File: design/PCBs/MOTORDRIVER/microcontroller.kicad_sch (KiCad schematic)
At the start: 0 parts

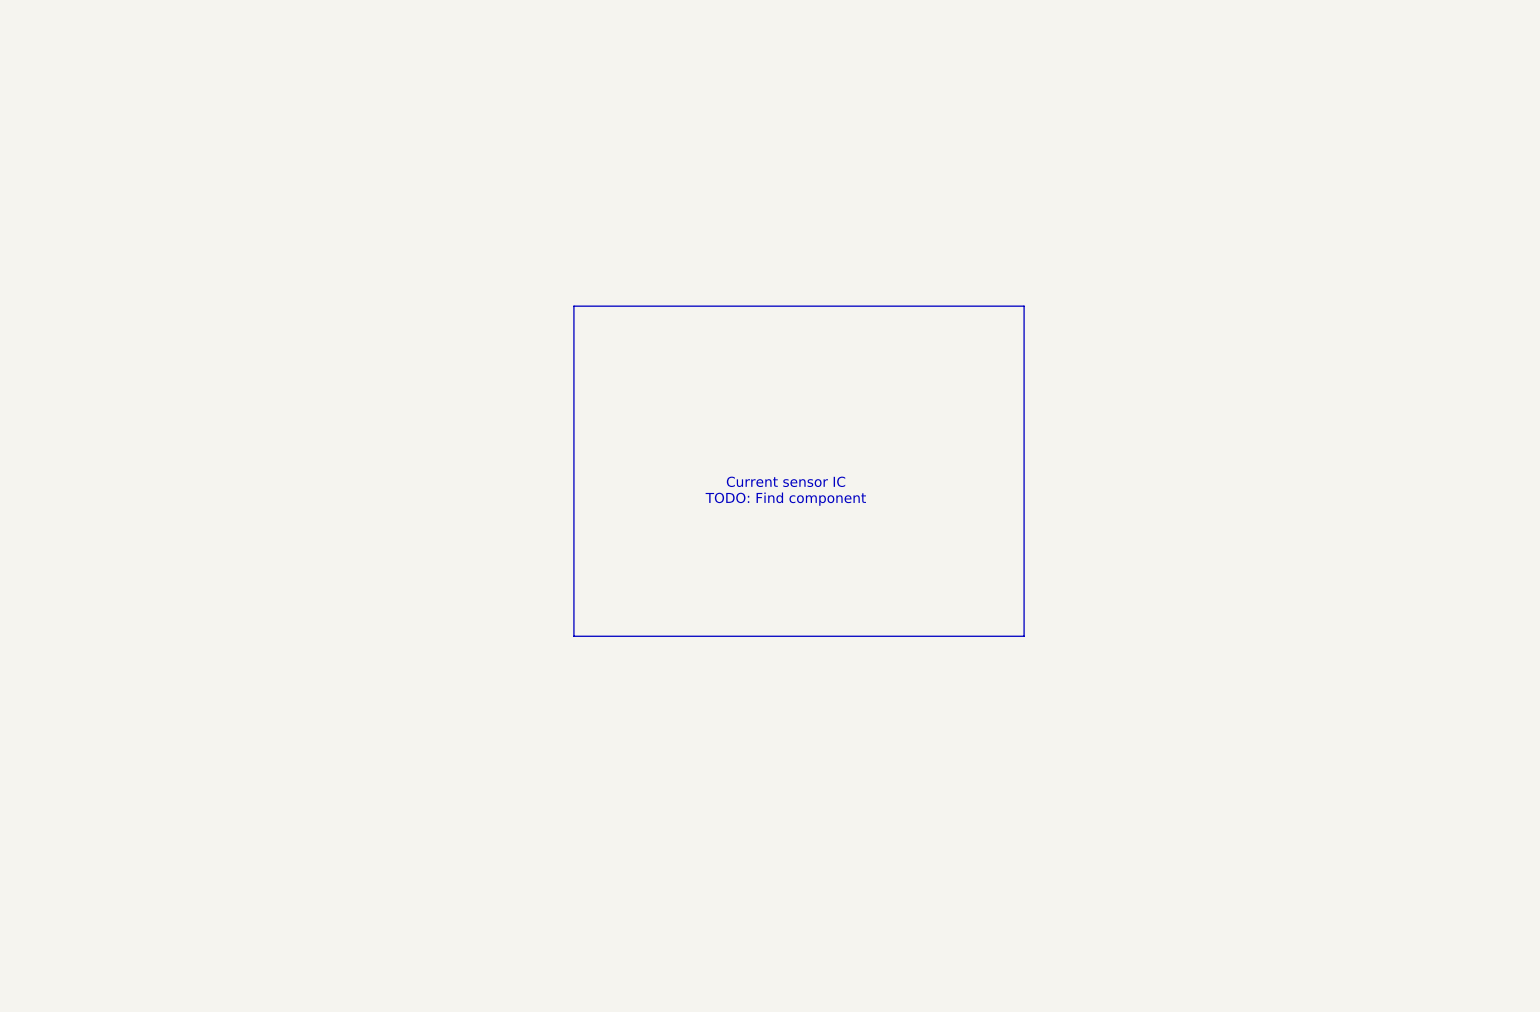
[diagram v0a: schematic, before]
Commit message: moved controller pcb to a single unified pcb, added more work on motordriver
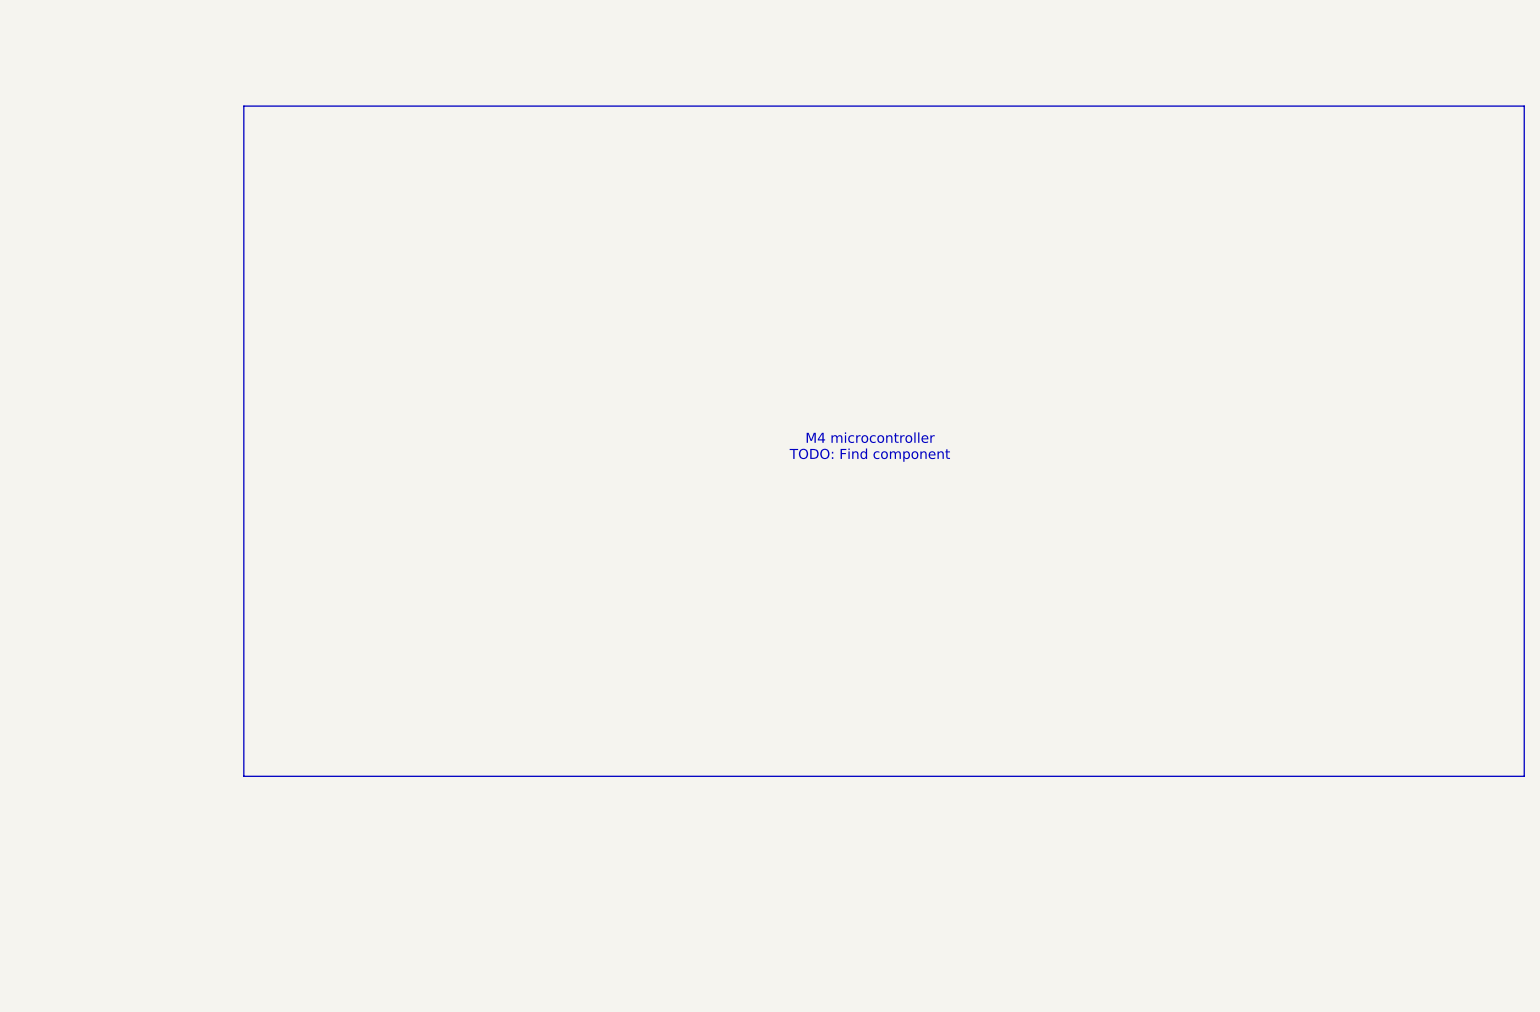
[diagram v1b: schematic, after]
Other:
- note added: "M4 microcontroller TODO: Find component"
- note removed: "Current sensor IC TODO: Find component"
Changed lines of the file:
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@@
 	(paper "A4")
 	(rectangle
-		(start 105.41 74.93)
-		(end 162.56 116.84)
+		(start 63.5 49.53)
+		(end 226.06 134.62)
 		(stroke
 			(width 0)
@@
 		)
 	)
-	(text "Current sensor IC\nTODO: Find component"
+	(text "M4 microcontroller\nTODO: Find component"
 		(exclude_from_sim no)
-		(at 132.334 98.552 0)
+		(at 143.002 92.964 0)
 		(effects
 			(font

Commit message: MCU added, x-ed some motordriver pins
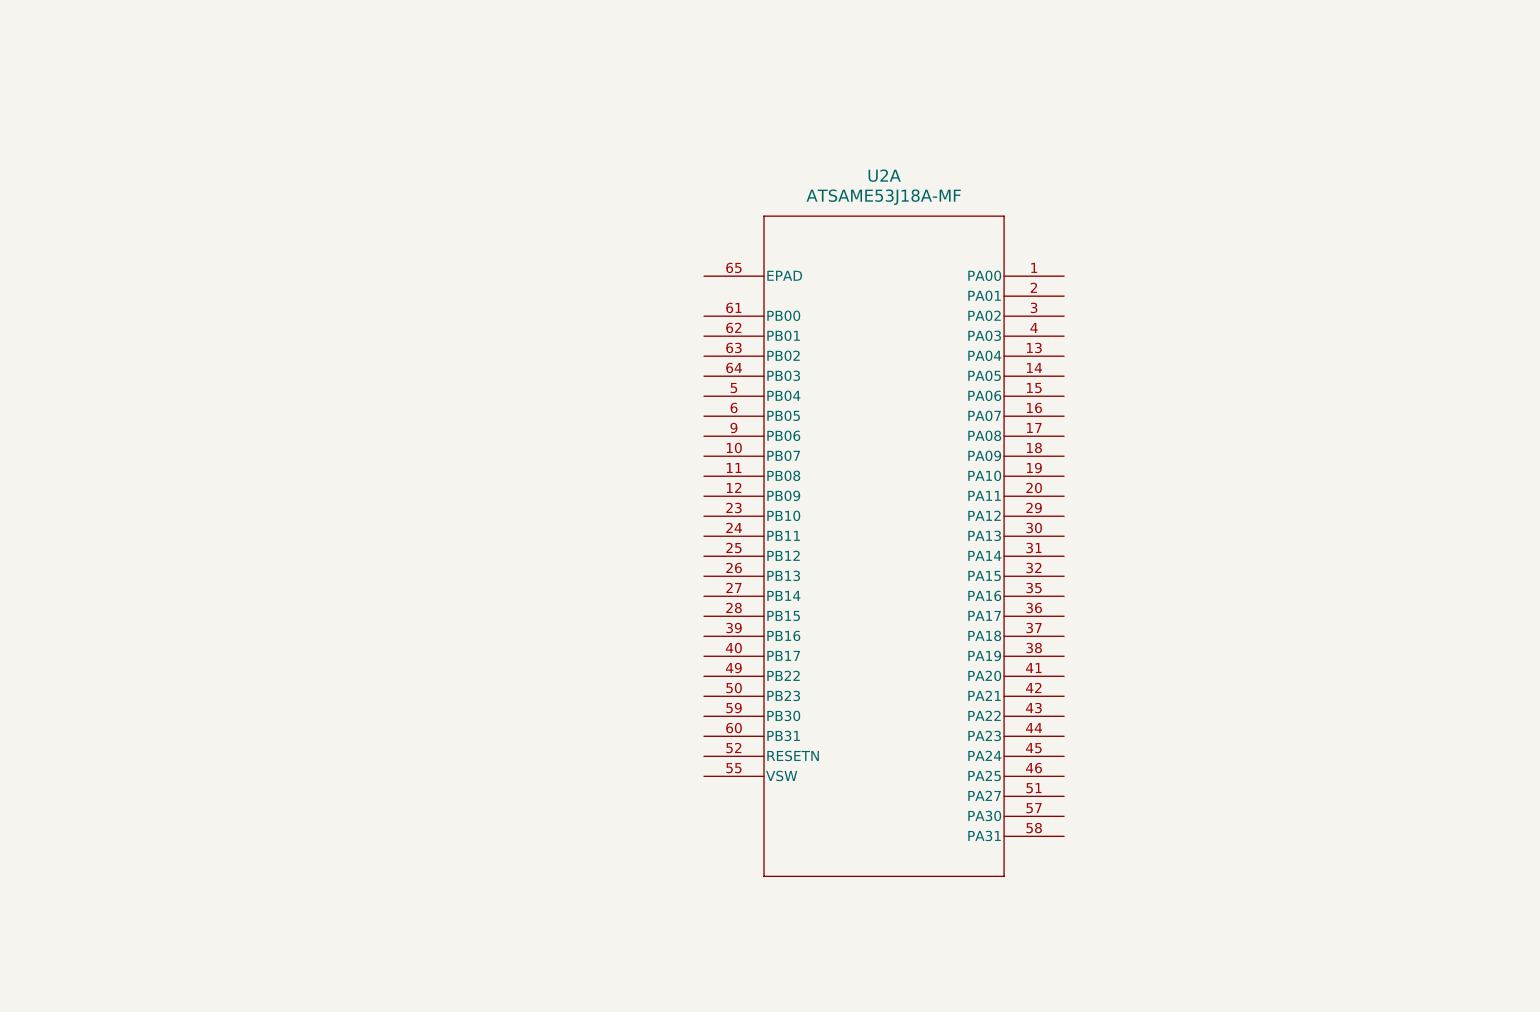
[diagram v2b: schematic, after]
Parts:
- added U2: ATSAME53J18A-MF, QFN64_9x9MC_MCH, symbol cortex-arm-m4:ATSAME53J18A-MF
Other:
- note removed: "M4 microcontroller TODO: Find component"
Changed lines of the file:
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@@
 	(generator_version "8.0")
 	(paper "A4")
-	(rectangle
-		(start 63.5 49.53)
-		(end 226.06 134.62)
-		(stroke
-			(width 0)
-			(type default)
-		)
-		(fill
-			(type none)
-		)
-	)
-	(text "M4 microcontroller\nTODO: Find component"
+	(symbol
+		(lib_id "cortex-arm-m4:ATSAME53J18A-MF")
+		(at 121.92 71.12 0)
+		(unit 1)
 		(exclude_from_sim no)
-		(at 143.002 92.964 0)
-		(effects
-			(font
-				(size 1.27 1.27)
+		(in_bom yes)
+		(on_board yes)
+		(dnp no)
+		(fields_autoplaced yes)
+		(property "Reference" "U2"
+			(at 144.78 58.42 0)
+			(effects
+				(font
+					(size 1.524 1.524)
+				)
 			)
 		)
+		(property "Value" "ATSAME53J18A-MF"
+			(at 144.78 60.96 0)
+			(effects
+				(font
+					(size 1.524 1.524)
+				)
+			)
+		)
+		(property "Footprint" "QFN64_9x9MC_MCH"
+			(at 121.92 71.12 0)
+			(effects
+				(font
+					(size 1.27 1.27)
+					(italic yes)
+				)
+				(hide yes)
+			)
+		)
+		(property "Datasheet" "ATSAME53J18A-MF"
+			(at 121.92 71.12 0)
+			(effects
+				(font
+					(size 1.27 1.27)
+					(italic yes)
+				)
+				(hide yes)
+			)
+		)
+		(property "Description" ""
+			(at 121.92 71.12 0)
+			(effects
+				(font
+					(size 1.27 1.27)
+				)
+				(hide yes)
+			)
+		)
+		(pin "60"
+		)
+		(pin "42"
+		)
+		(pin "59"
+		)
+		(pin "63"
+		)
+		(pin "50"
+		)
+		(pin "64"
+		)
+		(pin "62"
+		)
+		(pin "21"
+		)
+		(pin "61"
+		)
+		(pin "55"
+		)
+		(pin "65"
+		)
+		(pin "19"
+		)
+		(pin "22"
+		)
+		(pin "38"
+		)
+		(pin "52"
+		)
+		(pin "6"
+		)
+		(pin "18"
+		)
+		(pin "58"
+		)
+		(pin "1"
+		)
+		(pin "12"
+		)
+		(pin "11"
+		)
+		(pin "10"
+		)
+		(pin "2"
+		)
+		(pin "20"
+		)
+		(pin "57"
+		)
+		(pin "23"
+		)
+		(pin "44"
+		)
+		(pin "30"
+		)
+		(pin "13"
+		)
+		(pin "56"
+		)
+		(pin "43"
+		)
+		(pin "4"
+		)
+		(pin "32"
+		)
+		(pin "54"
+		)
+		(pin "15"
+		)
+		(pin "40"
+		)
+		(pin "8"
+		)
+		(pin "7"
+		)
+		(pin "45"
+		)
+		(pin "51"
+		)
+		(pin "3"
+		)
+		(pin "25"
+		)
+		(pin "27"
+		)
+		(pin "29"
+		)
+		(pin "33"
+		)
+		(pin "48"
+		)
+		(pin "14"
+		)
+		(pin "28"
+		)
+		(pin "53"
+		)
+		(pin "47"
+		)
+		(pin "34"
+		)
+		(pin "36"
+		)
+		(pin "49"
+		)
+		(pin "5"
+		)
+		(pin "46"
+		)
+		(pin "9"
+		)
+		(pin "26"
+		)
+		(pin "31"
+		)
+		(pin "35"
+		)
+		(pin "17"
+		)
+		(pin "37"
+		)
+		(pin "16"
+		)
+		(pin "24"
+		)
+		(pin "41"
+		)
+		(pin "39"
+		)
+		(instances
+			(project ""
+				(path "/c7634e88-16d1-45ec-9aac-9c841e03cf6d/9ebbb593-eaf1-4a56-ba2a-164e20b1d55e"
+					(reference "U2")
+					(unit 1)
+				)
+			)
+		)

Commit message: cortex added, fixed some symbols in motordriver file
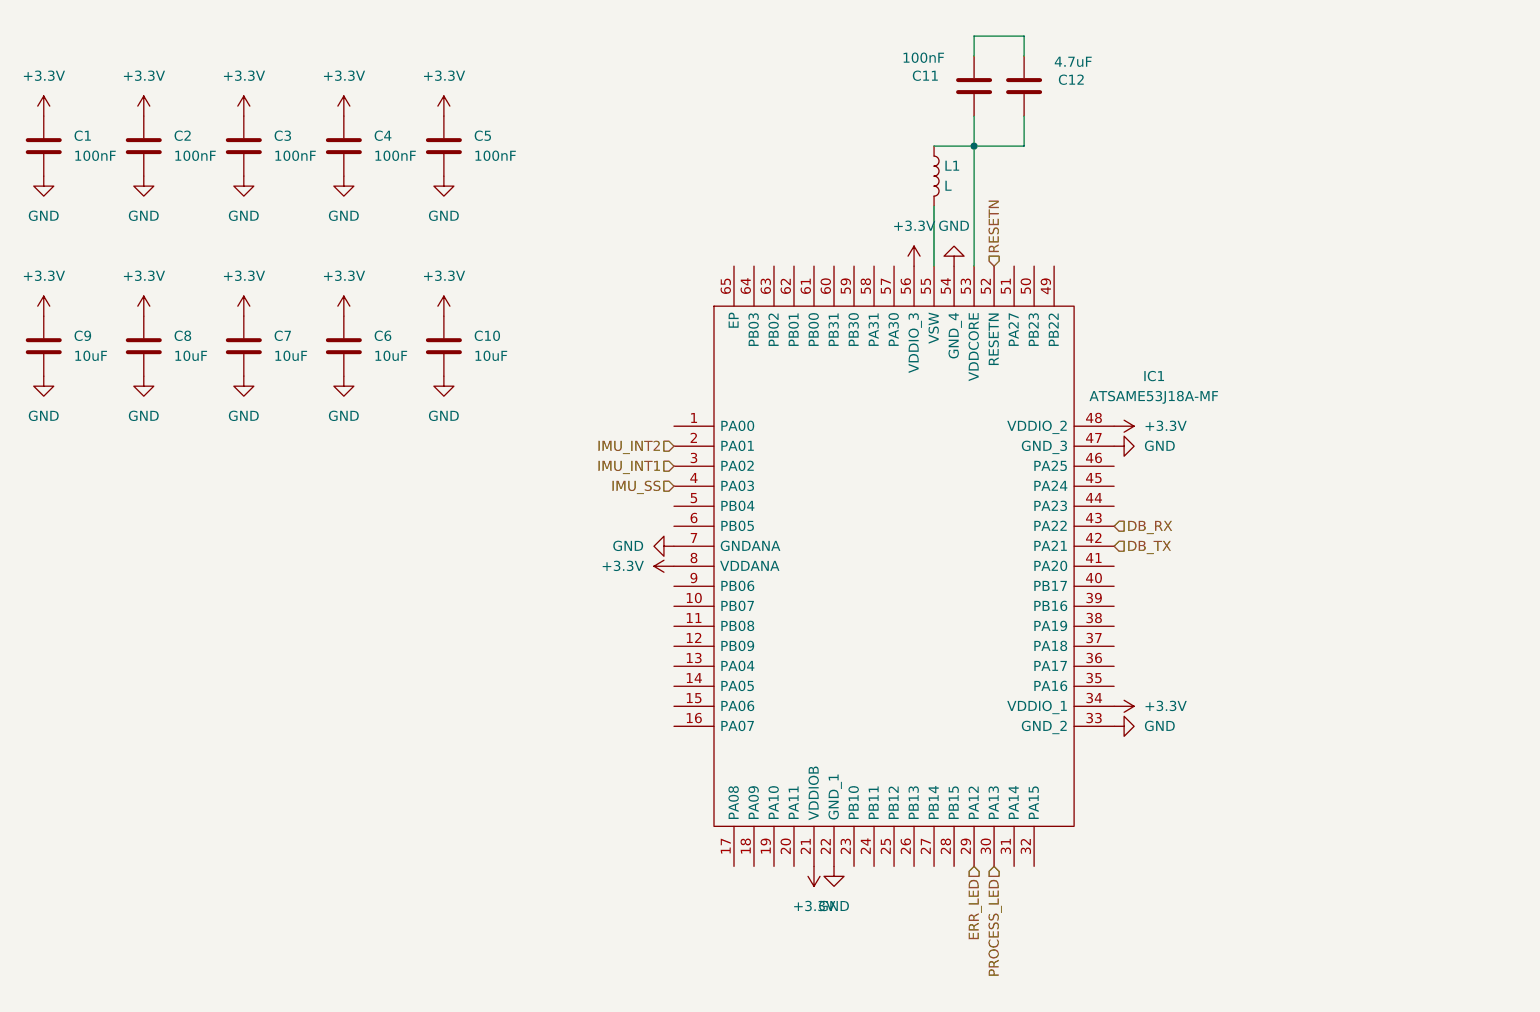
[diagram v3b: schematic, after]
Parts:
- removed U2: ATSAME53J18A-MF, QFN64_9x9MC_MCH, symbol cortex-arm-m4:ATSAME53J18A-MF
- added C1, C11, C2, C3, C4, C5: 100nF, symbol Device:C
- added C10, C6, C7, C8, C9: 10uF, symbol Device:C
- added C12: 4.7uF, symbol Device:C
- added IC1: ATSAME53J18A-MF, QFN50P900X900X100-65N-D, symbol ATSAME53J18A-MF:ATSAME53J18A-MF
- added L1: L, symbol Device:L
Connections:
- new net: C11.1, C12.1
- new net: C11.2, C12.2, IC1.53 (VDDCORE), L1.1
- new net: IC1.55 (VSW), L1.2
- new net +3.3V: C1.1, C10.1, C2.1, C3.1, C4.1, C5.1, C6.1, C7.1, C8.1, C9.1, IC1.21 (VDDIOB), IC1.34 (VDDIO_1), IC1.48 (VDDIO_2), IC1.56 (VDDIO_3), IC1.8 (VDDANA)
- new net DB_RX: IC1.43 (PA22)
- new net DB_TX: IC1.42 (PA21)
- new net ERR_LED: IC1.29 (PA12)
- new net GND: C1.2, C10.2, C2.2, C3.2, C4.2, C5.2, C6.2, C7.2, C8.2, C9.2, IC1.22 (GND_1), IC1.33 (GND_2), IC1.47 (GND_3), IC1.54 (GND_4), IC1.7 (GNDANA)
- new net IMU_INT1: IC1.3 (PA02)
- new net IMU_INT2: IC1.2 (PA01)
- new net IMU_SS: IC1.4 (PA03)
- new net PROCESS_LED: IC1.30 (PA13)
- new net RESETN: IC1.52 (RESETN)

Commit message: First draft of programmer added. GPIO pins are axed atm but can be included if we want some extra functionality, like indicator LEDs or similar.
Routing from USB-C to programmer to main cortex are added. Also
added some datasheets and sources.
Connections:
- net SWCLK: now reaches IC1.57 (PA30)
- net SWDIO: now reaches IC1.58 (PA31)
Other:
- note added: "to programmer"
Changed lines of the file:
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@@
+		)
+	)
+	(text "to programmer\n"
+		(exclude_from_sim no)
+		(at 144.526 54.356 90)
+		(effects
+			(font
+				(size 1.27 1.27)
+			)
 		)
 	)
@@
 		(fields_autoplaced yes)
 		(effects
+			(font
+				(size 1.27 1.27)
+			)
+			(justify left)
+		)
+	)
+	(hierarchical_label "SWDIO"
+		(shape input)
+		(at 143.51 69.85 90)
+		(fields_autoplaced yes)
+		(effects
+			(font
+				(size 1.27 1.27)
+			)
+			(justify left)
+		)
+	)
+	(hierarchical_label "SWCLK"
+		(shape input)
+		(at 146.05 69.85 90)
+		(fields_autoplaced yes)
+		(effects

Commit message: fixed schematic layout and added shunt resistor and zener diodes for motor stage
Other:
- note added: "Decoupling capacitors"
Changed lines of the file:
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@@
+		)
+	)
+	(text "Decoupling capacitors"
+		(exclude_from_sim no)
+		(at 65.532 39.624 0)
+		(effects
+			(font
+				(size 1.27 1.27)
+			)
 		)
 	)

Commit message: added oled header and connected to microcontroller. progress on vreg
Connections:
- net DB_RX: now also IC1.42 (PA21); no longer IC1.43 (PA22)
- net DB_TX: now also IC1.43 (PA22); no longer IC1.42 (PA21)
- net OLED_SCL: now reaches IC1.17 (PA08)
- net OLED_SDA: now reaches IC1.18 (PA09)
- net IMU2_SS: now reaches IC1.44 (PA23)
- net IMU2_INT1: now reaches IC1.45 (PA24)
- net IMU2_INT2: now reaches IC1.46 (PA25)
- net IMU_INT1 renamed IMU1_INT1
- net IMU_INT2 renamed IMU1_INT2
- net IMU_SS renamed IMU1_SS
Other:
- note added: "assuming i2c screen"
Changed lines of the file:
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@@
+		)
+	)
+	(text "assuming i2c screen"
+		(exclude_from_sim no)
+		(at 127.762 159.512 0)
+		(effects
+			(font
+				(size 1.27 1.27)
+			)
 		)
 	)
@@
 		)
 	)
-	(hierarchical_label "DB_TX"
+	(hierarchical_label "DB_RX"
 		(shape input)
 		(at 173.99 105.41 0)
@@
 		)
 	)
-	(hierarchical_label "DB_RX"
+	(hierarchical_label "DB_TX"
 		(shape input)
 		(at 173.99 102.87 0)
@@
 		)
 	)
+	(hierarchical_label "IMU2_INT1"
+		(shape input)
+		(at 173.99 97.79 0)
+		(fields_autoplaced yes)
+		(effects
+			(font
+				(size 1.27 1.27)
+			)
+			(justify left)
+		)
+	)
 	(hierarchical_label "SWDIO"
 		(shape input)
@@
 		)
 	)
+	(hierarchical_label "OLED_SCL"
+		(shape input)
+		(at 125.73 146.05 270)
+		(fields_autoplaced yes)
+		(effects
+			(font
+				(size 1.27 1.27)
+			)
+			(justify right)
+		)
+	)
+	(hierarchical_label "IMU2_INT2"
+		(shape input)
+		(at 173.99 95.25 0)
+		(fields_autoplaced yes)
+		(effects
+			(font
+				(size 1.27 1.27)
+			)
+			(justify left)
+		)
+	)
 	(hierarchical_label "PROCESS_LED"
 		(shape input)
@@
 		)
 	)
-	(hierarchical_label "IMU_SS"
+	(hierarchical_label "IMU2_SS"
 		(shape input)
-		(at 118.11 97.79 180)
+		(at 173.99 100.33 0)
 		(fields_autoplaced yes)
 		(effects
@@
 				(size 1.27 1.27)
 			)
-			(justify right)
-		)
-	)
-	(hierarchical_label "IMU_INT1"
+			(justify left)
+		)
+	)
+	(hierarchical_label "IMU1_SS"
 		(shape input)
-		(at 118.11 95.25 180)
+		(at 118.11 97.79 180)
 		(fields_autoplaced yes)
 		(effects
@@
 		)
 	)
-	(hierarchical_label "IMU_INT2"
+	(hierarchical_label "IMU1_INT1"
 		(shape input)
-		(at 118.11 92.71 180)
+		(at 118.11 95.25 180)
 		(fields_autoplaced yes)
 		(effects
@@
 		)
 	)
+	(hierarchical_label "OLED_SDA"
+		(shape input)
+		(at 128.27 146.05 270)
+		(fields_autoplaced yes)
+		(effects
+			(font
+				(size 1.27 1.27)
+			)
+			(justify right)
+		)
+	)
+	(hierarchical_label "IMU1_INT2"
+		(shape input)
+		(at 118.11 92.71 180)
+		(fields_autoplaced yes)
+		(effects
+			(font
+				(size 1.27 1.27)
+			)
+			(justify right)
+		)
+	)
 	(symbol
 		(lib_id "Device:C")
@@
 		(on_board yes)
 		(dnp no)
-		(fields_autoplaced yes)
 		(property "Reference" "#PWR056"
 			(at 138.43 152.4 0)
@@
 		)
 		(property "Value" "GND"
-			(at 138.43 151.13 0)
+			(at 138.43 151.13 90)
 			(effects
 				(font
@@
 		(on_board yes)
 		(dnp no)
-		(fields_autoplaced yes)
 		(property "Reference" "#PWR057"
 			(at 135.89 142.24 0)
@@
 		)
 		(property "Value" "+3.3V"
-			(at 135.89 151.13 0)
-			(effects
-				(font
+			(at 135.89 152.4 90)
+			(effects
+				(font
